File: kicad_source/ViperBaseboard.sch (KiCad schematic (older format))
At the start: 5 parts, among them CN1 ARDUINO_MKR

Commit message: updated layout, added step of baseboard
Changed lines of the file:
@@
 $Descr A4 11693 8268
 encoding utf-8
-Sheet 1 3
+Sheet 1 4
 Title "ViperBaseboard"
 Date "2020-04-02"
@@
 Text Label 4900 3800 0    50   ~ 0
 SER_TX
+$Sheet
+S 9500 3500 1000 500
+U 5E85D0D5
+F0 "IMU" 50
+F1 "imu.sch" 50
+$EndSheet
 $EndSCHEMATC

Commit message: redefined shape of PCB
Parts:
- CN1: footprint MODULE_compute:ARDUINO_MKR -> MODULE_compute:ARDUINO_MKR_BASEBOARD
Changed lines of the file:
@@
 F 0 "CN1" H 3550 4847 60  0000 C CNN
 F 1 "ARDUINO_MKR" H 3550 4741 60  0000 C CNN
-F 2 "MODULE_compute:ARDUINO_MKR" H 3450 4600 60  0001 C CNN
+F 2 "MODULE_compute:ARDUINO_MKR_BASEBOARD" H 3450 4600 60  0001 C CNN
 F 3 "" H 3550 3650 60  0000 C CNN
 	1    3550 3950

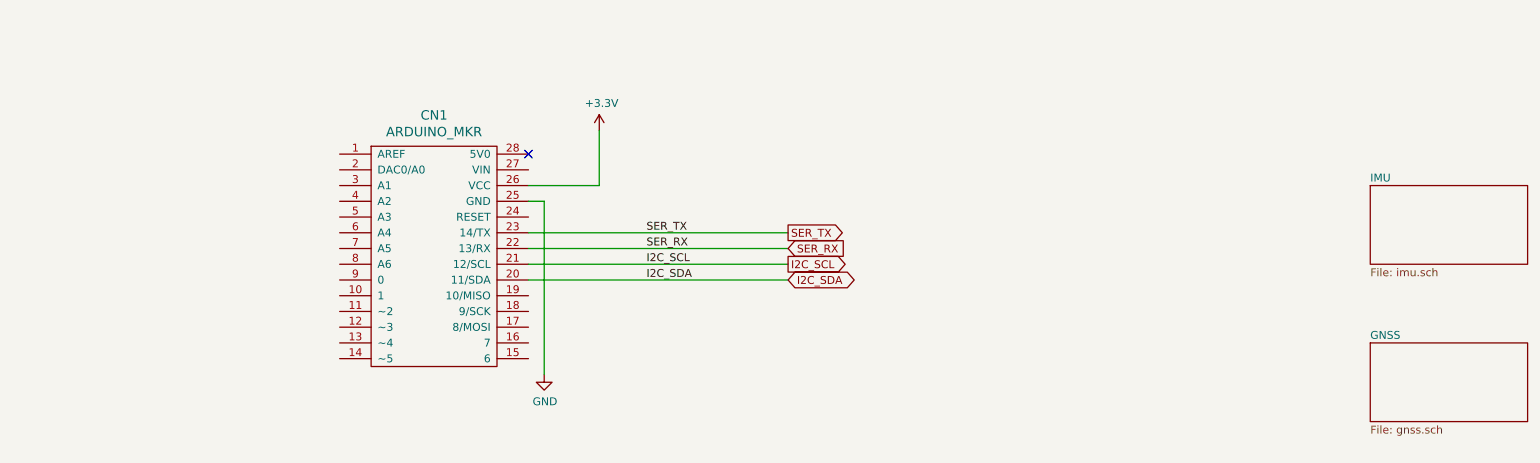
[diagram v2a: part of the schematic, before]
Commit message: added schematic sheet with MCP2515
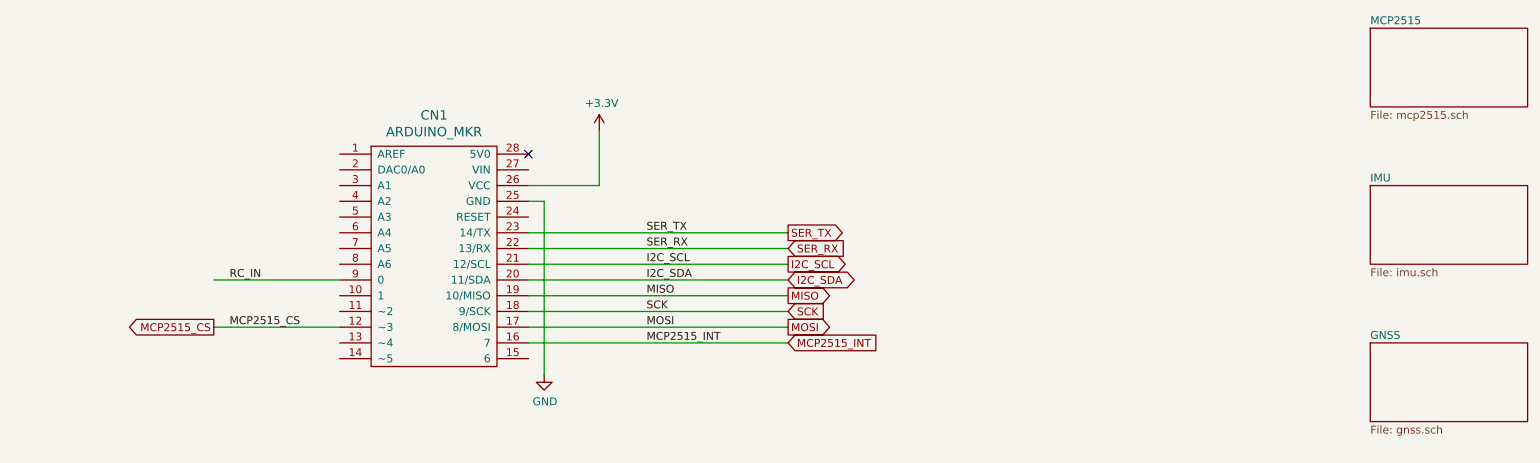
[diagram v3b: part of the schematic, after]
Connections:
- net labels added: MCP2515_CS, MCP2515_INT, MISO, MOSI, RC_IN, SCK
- wire segments 8 -> 14
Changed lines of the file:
@@
 $Descr A4 11693 8268
 encoding utf-8
-Sheet 1 4
+Sheet 1 5
 Title "ViperBaseboard"
 Date "2020-04-02"
@@
 F1 "imu.sch" 50
 $EndSheet
+Wire Wire Line
+	5800 4500 4150 4500
+Wire Wire Line
+	5800 4400 4150 4400
+Text Label 4900 4500 0    50   ~ 0
+MCP2515_INT
+Text Label 4900 4400 0    50   ~ 0
+MOSI
+Text GLabel 5800 4500 2    50   Input ~ 0
+MCP2515_INT
+Text GLabel 5800 4400 2    50   Output ~ 0
+MOSI
+Text GLabel 5800 4300 2    50   Input ~ 0
+SCK
+Text GLabel 5800 4200 2    50   Output ~ 0
+MISO
+Wire Wire Line
+	5800 4200 4150 4200
+Wire Wire Line
+	4150 4300 5800 4300
+Text Label 4900 4300 0    50   ~ 0
+SCK
+Text Label 4900 4200 0    50   ~ 0
+MISO
+Wire Wire Line
+	2150 4100 2950 4100
+Text Label 2250 4100 0    50   ~ 0
+RC_IN
+Wire Wire Line
+	2150 4400 2950 4400
+Text Label 2250 4400 0    50   ~ 0
+MCP2515_CS
+Text GLabel 2150 4400 0    50   Output ~ 0
+MCP2515_CS
+$Sheet
+S 9500 2500 1000 500
+U 5ED92F9C
+F0 "MCP2515" 50
+F1 "mcp2515.sch" 50
+$EndSheet
 $EndSCHEMATC

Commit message: added schematic sheet with sd-card
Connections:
- net labels added: SD_CS
- wire segments 14 -> 15
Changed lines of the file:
@@
 $Descr A4 11693 8268
 encoding utf-8
-Sheet 1 5
+Sheet 1 6
 Title "ViperBaseboard"
 Date "2020-04-02"
@@
 F1 "mcp2515.sch" 50
 $EndSheet
+$Sheet
+S 9500 1500 1000 500
+U 5EDB73FA
+F0 "SD-Card" 50
+F1 "sd-card.sch" 50
+$EndSheet
+Wire Wire Line
+	2150 4500 2950 4500
+Text Label 2250 4500 0    50   ~ 0
+SD_CS
+Text GLabel 2150 4500 0    50   Output ~ 0
+SD_CS
 $EndSCHEMATC
